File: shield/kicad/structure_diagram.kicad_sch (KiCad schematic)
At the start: 49 parts, among them J10 QR_FFC, J11 Arduino_D8-D13, J12 Arduino_D0-D7, J13 Arduino_Analog, J8 Smartcard, J9 Conn_01x08, U6 ST8034

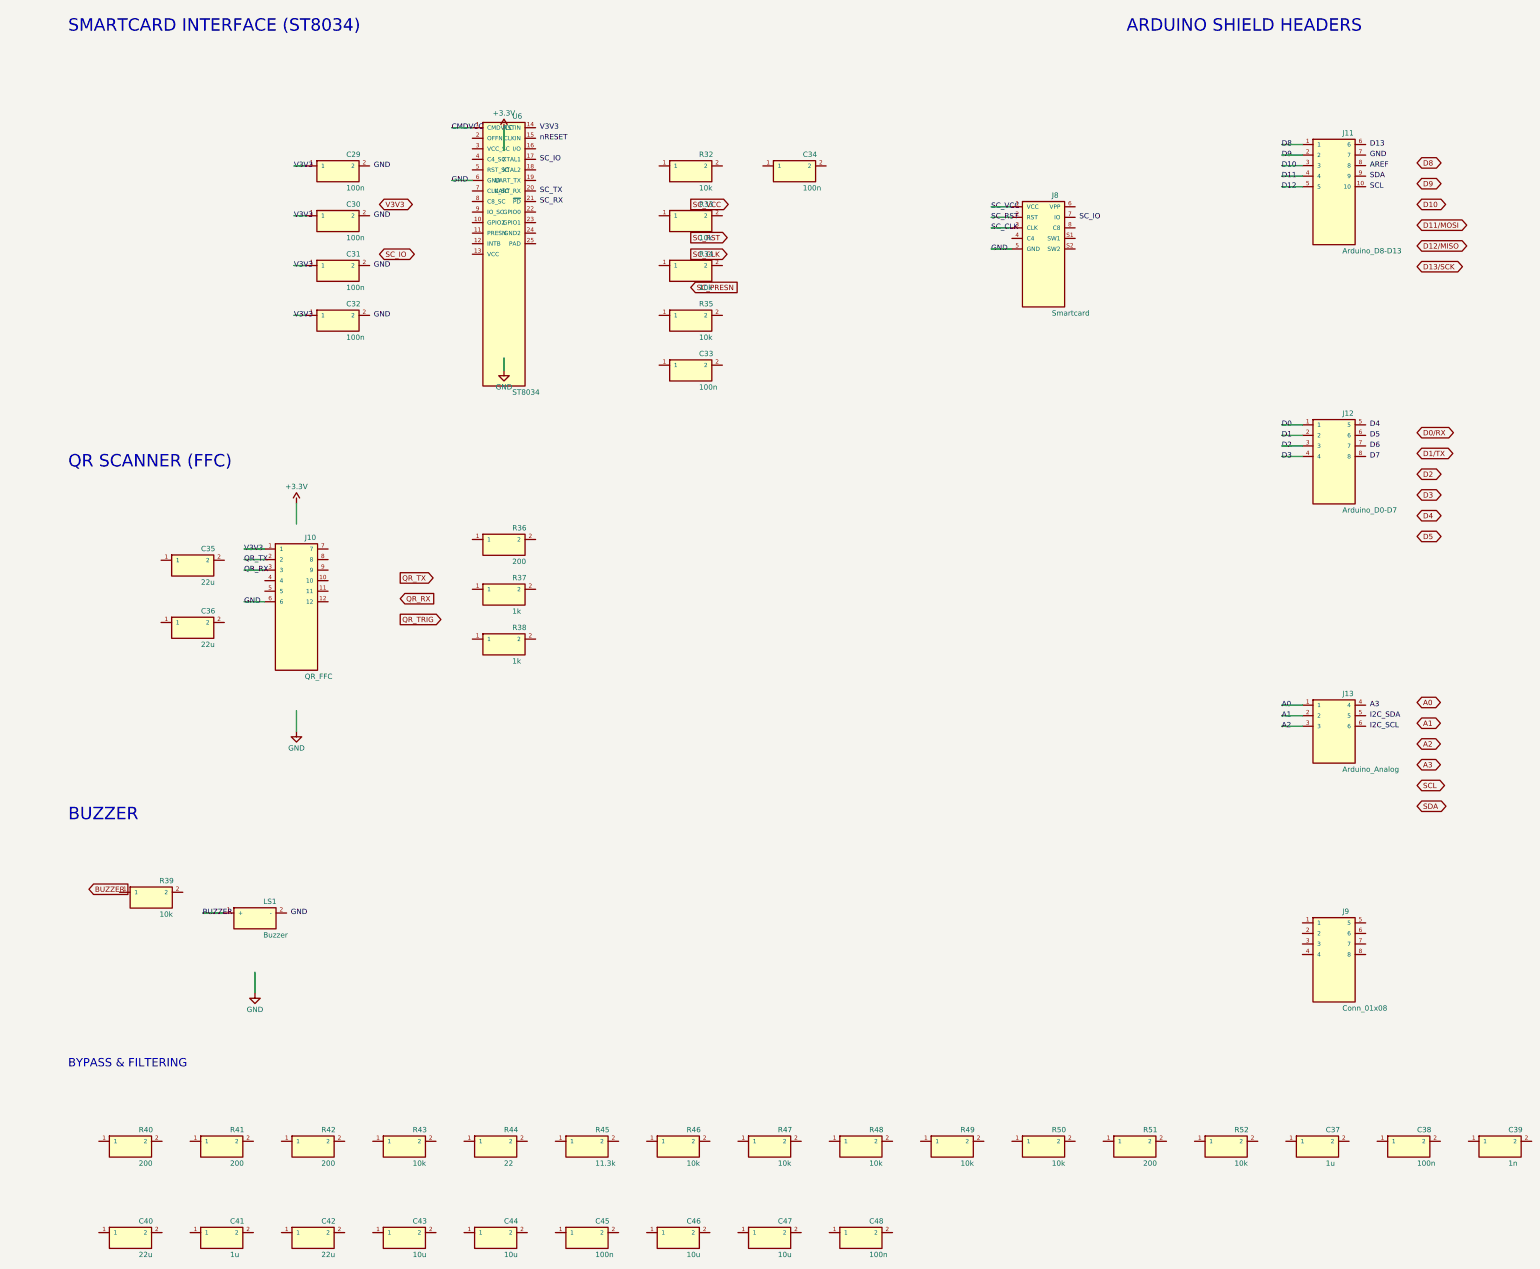
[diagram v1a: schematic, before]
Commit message: Add descriptive text blocks to all schematic sheets describing functional blocks
- Main sheet: board overview, sub-sheet summaries, and design notes
- Power sheet: USB input, charger, fuel gauge, buck-boost, supervisor, power control descriptions
- Peripherals sheet: smartcard, QR scanner, Arduino headers, buzzer, bypass descriptions
- Re-rendered all schematic and PCB images with kicad-cli-nightly

Agent-Logs-Url: https://github.com/3rdIteration/specter-diy/sessions/73613ef4-1004-4e39-bea0-e2793e248b2a

Co-authored-by: 3rdIteration <2230318+3rdIteration@users.noreply.github.com>
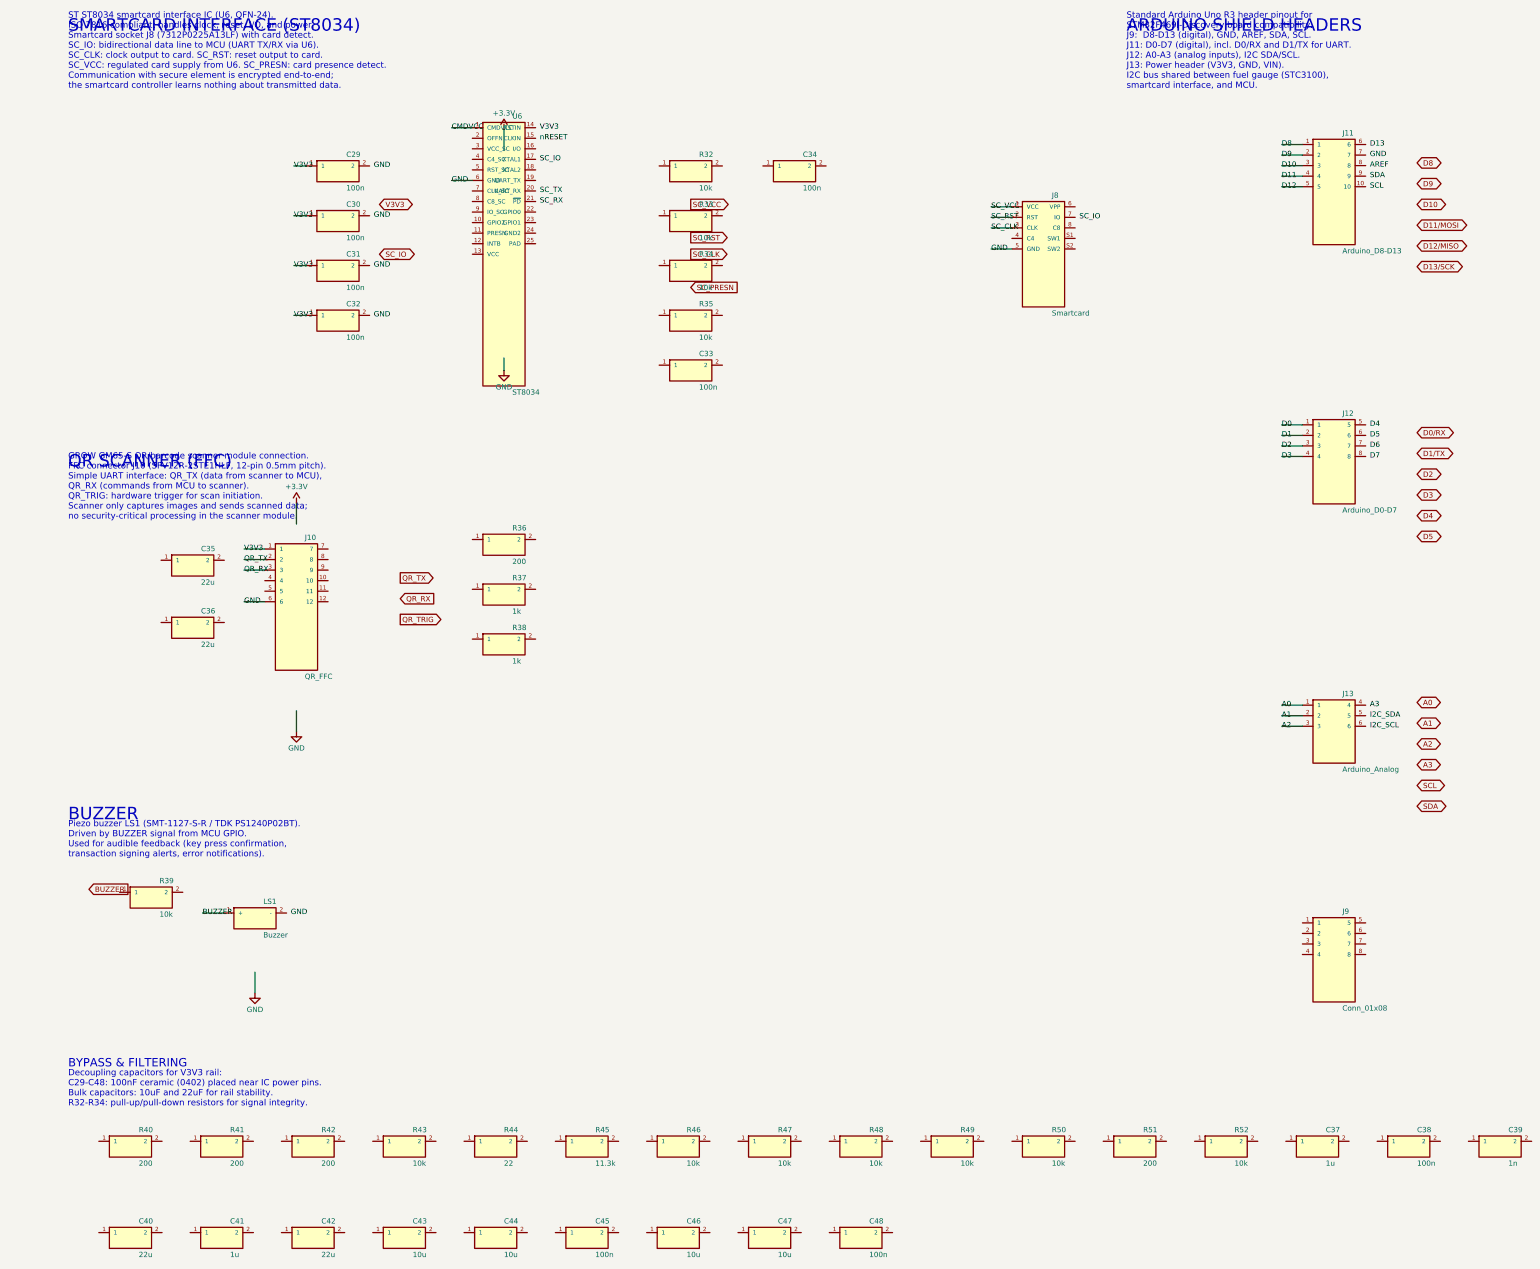
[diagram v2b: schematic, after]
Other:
- note added: "Decoupling capacitors for V3V3 rail: C29-C48: 100nF ceramic (0402) placed near IC power pins. Bulk capacitors: 10uF and 22uF for rail stability. R32-R34: pull-up/pull-down resistors for signal integrity."
- note added: "GROW GM65-S QR/barcode scanner module connection. FFC connector J10 (SFV12R-2STE1HLF, 12-pin 0.5mm pitch). Simple UART interface: QR_TX (data from scanner to MCU), QR_RX (commands from MCU to scanner). QR_TRIG: hardware trigger for scan initiation. Scanner only captures images and sends scanned data; no security-critical processing in the scanner module."
- note added: "Piezo buzzer LS1 (SMT-1127-S-R / TDK PS1240P02BT). Driven by BUZZER signal from MCU GPIO. Used for audible feedback (key press confirmation, transaction signing alerts, error notifications)."
- note added: "ST ST8034 smartcard interface IC (U6, QFN-24). ISO 7816 compliant: handles clock, reset, I/O, and power. Smartcard socket J8 (7312P0225A13LF) with card detect. SC_IO: bidirectional data line to MCU (UART TX/RX via U6). SC_CLK: clock output to card. SC_RST: reset output to card. SC_VCC: regulated card supply from U6. SC_PRESN: card presence detect. Communication with secure element is encrypted en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"
- note added: "Standard Arduino Uno R3 header pinout for STM32F469I-Discovery board compatibility. J9: D8-D13 (digital), GND, AREF, SDA, SCL. J11: D0-D7 (digital), incl. D0/RX and D1/TX for UART. J12: A0-A3 (analog inputs), I2C SDA/SCL. J13: Power header (V3V3, GND, VIN). I2C bus shared between fuel gauge (STC3100), smartcard interface, and MCU."
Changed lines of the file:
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@@
 		(title "Specter Shield v1 - Peripherals & Connectors")
 	)
-	(text "SMARTCARD INTERFACE (ST8034)"
-		(exclude_from_sim no)
-		(at 25 25 0)
-		(effects
-			(font
-				(size 3 3)
-			)
-			(justify left)
-		)
-	)
-	(text "QR SCANNER (FFC)"
-		(exclude_from_sim no)
-		(at 25 130 0)
-		(effects
-			(font
-				(size 3 3)
-			)
-			(justify left)
-		)
-	)
-	(text "ARDUINO SHIELD HEADERS"
-		(exclude_from_sim no)
-		(at 280 25 0)
-		(effects
-			(font
-				(size 3 3)
-			)
-			(justify left)
-		)
-	)
-	(text "BUZZER"
-		(exclude_from_sim no)
-		(at 25 215 0)
-		(effects
-			(font
-				(size 3 3)
-			)
-			(justify left)
-		)
-	)
-	(text "BYPASS & FILTERING"
-		(exclude_from_sim no)
-		(at 25 275 0)
-		(effects
-			(font
-				(size 2 2)
-			)
-			(justify left)
-		)
-	)
 	(wire
 		(pts
@@
 			)
 			(justify left)
+		)
+	)
+	(text "SMARTCARD INTERFACE (ST8034)"
+		(exclude_from_sim no)
+		(at 25 25 0)
+		(effects
+			(font
+				(size 3 3)
+			)
+			(justify left)
+		)
+	)
+	(text "ST ST8034 smartcard interface IC (U6, QFN-24).\nISO 7816 compliant: handles clock, reset, I/O, and power.\nSmartcard socket J8 (7312P0225A13LF) with card detect.\nSC_IO: bidirectional data line to MCU (UART TX/RX via U6).\nSC_CLK: clock output to card. SC_RST: reset output to card.\nSC_VCC: regulated card supply from U6. SC_PRESN: card presence detect.\nCommunication with secure element is encrypted end-to-end;\nthe smartcard controller learns nothing about transmitted data."
+		(exclude_from_sim no)
+		(at 25 31 0)
+		(effects
+			(font
+				(size 1.5 1.5)
+				(color 0 0 150 1)
+			)
+			(justify left)
+		)
+	)
+	(text "QR SCANNER (FFC)"
+		(exclude_from_sim no)
+		(at 25 130 0)
+		(effects
+			(font
+				(size 3 3)
+			)
+			(justify left)
+		)
+	)
+	(text "GROW GM65-S QR/barcode scanner module connection.\nFFC connector J10 (SFV12R-2STE1HLF, 12-pin 0.5mm pitch).\nSimple UART interface: QR_TX (data from scanner to MCU),\nQR_RX (commands from MCU to scanner).\nQR_TRIG: hardware trigger for scan initiation.\nScanner only captures images and sends scanned data;\nno security-critical processing in the scanner module."
+		(exclude_from_sim no)
+		(at 25 136 0)
+		(effects
+			(font
+				(size 1.5 1.5)
+				(color 0 0 150 1)
+			)
+			(justify left)
+		)
+	)
+	(text "ARDUINO SHIELD HEADERS"
+		(exclude_from_sim no)
+		(at 280 25 0)
+		(effects
+			(font
+				(size 3 3)
+			)
+			(justify left)
+		)
+	)
+	(text "Standard Arduino Uno R3 header pinout for\nSTM32F469I-Discovery board compatibility.\nJ9:  D8-D13 (digital), GND, AREF, SDA, SCL.\nJ11: D0-D7 (digital), incl. D0/RX and D1/TX for UART.\nJ12: A0-A3 (analog inputs), I2C SDA/SCL.\nJ13: Power header (V3V3, GND, VIN).\nI2C bus shared between fuel gauge (STC3100),\nsmartcard interface, and MCU."
+		(exclude_from_sim no)
+		(at 280 31 0)
+		(effects
+			(font
+				(size 1.5 1.5)
+				(color 0 0 150 1)
+			)
+			(justify left)
+		)
+	)
+	(text "BUZZER"
+		(exclude_from_sim no)
+		(at 25 215 0)
+		(effects
+			(font
+				(size 3 3)
+			)
+			(justify left)
+		)
+	)
+	(text "Piezo buzzer LS1 (SMT-1127-S-R / TDK PS1240P02BT).\nDriven by BUZZER signal from MCU GPIO.\nUsed for audible feedback (key press confirmation,\ntransaction signing alerts, error notifications)."
+		(exclude_from_sim no)
+		(at 25 221 0)
+		(effects
+			(font
+				(size 1.5 1.5)
+				(color 0 0 150 1)
+			)
+			(justify left)
+		)
+	)
+	(text "BYPASS & FILTERING"
+		(exclude_from_sim no)
+		(at 25 275 0)
+		(effects
+			(font
+				(size 2 2)
+			)
+			(justify left)
+		)
+	)
+	(text "Decoupling capacitors for V3V3 rail:\nC29-C48: 100nF ceramic (0402) placed near IC power pins.\nBulk capacitors: 10uF and 22uF for rail stability.\nR32-R34: pull-up/pull-down resistors for signal integrity."
+		(exclude_from_sim no)
+		(at 25 281 0)
+		(effects
+			(font
+				(size 1.5 1.5)
+				(color 0 0 150 1)
+			)
+			(justify left)
